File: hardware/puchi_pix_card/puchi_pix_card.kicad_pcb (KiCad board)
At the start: 4 copper layers, 54 x 54 mm, 366 parts, among them J1 USB_C_Receptacle_USB2.0_16P, J2 Conn_01x04, Q101 AO3401A, Q102 AO3401A, Q103 AO3401A, Q104 AO3401A, Q105 AO3401A, Q106 AO3401A, Q107 AO3401A, Q108 AO3401A, Q109 AO3401A, Q110 AO3401A, Q111 AO3401A, Q112 AO3401A, Q113 AO3401A, Q114 AO3401A, Q115 AO3401A, Q116 AO3401A, SW1 VBAT_SW, SW2 SW_Push, SW3 SW_Push, U1 TPS61023DRL, U101 MBI5153GP (R), U102 MBI5153GP (G), U103 MBI5153GP (B), U104 74HCT595, U105 74HCT595, U2 XC6206PxxxMR, U3 STM32G0B1CBTx, U4 XC6206PxxxMR, U5 USBLC6-2SC6, U6 KXTJ3-1057, U7 W25Q64JVSSIQ

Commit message: Swap J2 to JST SH with v1 power pin order (1:GND 2:+3V3S); replace the battery symbol with four pogo-pin contacts (VBAT/GND)
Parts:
- added BT1: POGO BT+, puchi_pix_card:Pogo_YTC1P_D2.0, B.Cu at (151.8, 105.4)
- added BT2: POGO BT+, puchi_pix_card:Pogo_YTC1P_D2.0, B.Cu at (151.8, 108.5)
- added BT3: POGO BT-, puchi_pix_card:Pogo_YTC1P_D2.0, B.Cu at (102.0, 140.5)
- added BT4: POGO BT-, puchi_pix_card:Pogo_YTC1P_D2.0, B.Cu at (102.0, 143.5)
- J2: value Conn_01x04 -> SWD (JST SH 4P); footprint Connector_PinHeader_2.54mm:PinHeader_1x04_P2.54mm_Vertical_SMD_Pin1Left -> JST_SH_SM04B-SRSS-TB_1x04-1MP_P1.00mm_Horizontal
- moved R120 3.83 mm to (143.6, 109.2), turned to 0 degrees
- moved Q102 2.88 mm to (144.6, 105.8)
- moved Q103 2.74 mm to (148.5, 107.2)
- moved R119 2.20 mm to (142.9, 108.1), turned to 0 degrees
- turned J2 to 90 degrees
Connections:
- C14 pad 1: Net-(J2-Pin_1) -> +3V3S
- C5 pad 1: Net-(J2-Pin_1) -> +3V3S
- C6 pad 1: Net-(J2-Pin_1) -> +3V3S
- C7 pad 1: Net-(J2-Pin_1) -> +3V3S
- C8 pad 1: Net-(J2-Pin_1) -> +3V3S
- J2 pad 1: Net-(J2-Pin_1) -> GND
- J2 pad 2: /mcu/SWDIO -> +3V3S
- J2 pad 3: /mcu/BOOT/SWCLK -> /mcu/SWDIO
- J2 pad 4: GND -> /mcu/BOOT/SWCLK
- R13 pad 1: Net-(J2-Pin_1) -> +3V3S
- R14 pad 1: Net-(J2-Pin_1) -> +3V3S
- SW1 pad 2: Net-(BT1-+) -> VBAT
- SW3 pad 2: Net-(J2-Pin_1) -> +3V3S
- U2 pad 2: Net-(J2-Pin_1) -> +3V3S
- U3 pad 4: Net-(J2-Pin_1) -> +3V3S
- U3 pad 5: Net-(J2-Pin_1) -> +3V3S
- U3 pad 6: Net-(J2-Pin_1) -> +3V3S
- U6 pad 10: Net-(J2-Pin_1) -> +3V3S
- U6 pad 11: Net-(J2-Pin_1) -> +3V3S
- U6 pad 3: Net-(J2-Pin_1) -> +3V3S
- U6 pad 7: Net-(J2-Pin_1) -> +3V3S
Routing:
- net +3V3S: track 0.00 -> 107.7 mm, vias 0 -> 5
- net Net-(J2-Pin_1): track 103.2 -> 0.00 mm, vias 5 -> 0
- net VBAT: track 0.00 -> 27.5 mm, vias 0 -> 2
- net GND: track 160.2 -> 166.7 mm, vias 24 -> 25
- net +5V: track 434.1 -> 430.4 mm
- net /mcu/BOOT/SWCLK: track 80.2 -> 83.9 mm
- net /display/COL_R15: track 58.2 -> 61.1 mm
- net /display/ROW2: track 60.2 -> 62.9 mm
- net /mcu/SWDIO: track 45.6 -> 47.5 mm
- net /display/SR_Q1: track 15.3 -> 16.5 mm
- net Net-(U101-OUT14): track 30.5 -> 29.5 mm
- net Net-(U101-OUT15): track 34.0 -> 33.2 mm
- net /display/SR_Q2: track 21.8 -> 21.0 mm

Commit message: Fill LCSC part numbers for JLCPCB assembly; switch the column drivers to MBI5124GP-B (pin 21 GCLK -> /OE, net MBI_OE); R2 133k, in-stock LED/NOR listings
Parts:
- J1: value USB_C_Receptacle_USB2.0_16P -> TYPE-C 16P QTWT
- R2: value 135k -> 133k
- U101: value MBI5153GP (R) -> MBI5124GP-B (R)
- U102: value MBI5153GP (G) -> MBI5124GP-B (G)
- U103: value MBI5153GP (B) -> MBI5124GP-B (B)
- U2, U4: value XC6206PxxxMR -> XC6206P332MR
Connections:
- net GCLK renamed MBI_OE

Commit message: Review fixes: guard the first plane against ISR re-entry, SPI2 8 MHz for the 3.3V chain delay, release the KXTJ3 latched INT, force /OE high on stop; J2 real part name and footprint id; drop MBI5153 leftovers
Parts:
- J2: value SWD (JST SH 4P) -> SWD XDWF-0910-04P (JST SH compatible); footprint JST_SH_SM04B-SRSS-TB_1x04-1MP_P1.00mm_Horizontal -> Connector_JST:JST_SH_SM04B-SRSS-TB_1x04-1MP_P1.00mm_Horizontal
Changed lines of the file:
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@@
 		)
 	)
-	(footprint "JST_SH_SM04B-SRSS-TB_1x04-1MP_P1.00mm_Horizontal"
+	(footprint "Connector_JST:JST_SH_SM04B-SRSS-TB_1x04-1MP_P1.00mm_Horizontal"
 		(layer "B.Cu")
 		(at 103.75 106.61 90)
@@
 			)
 		)
-		(property "Value" "SWD (JST SH 4P)"
+		(property "Value" "SWD XDWF-0910-04P (JST SH compatible)"
 			(at 0 -3.98 270)
 			(layer "B.Fab")

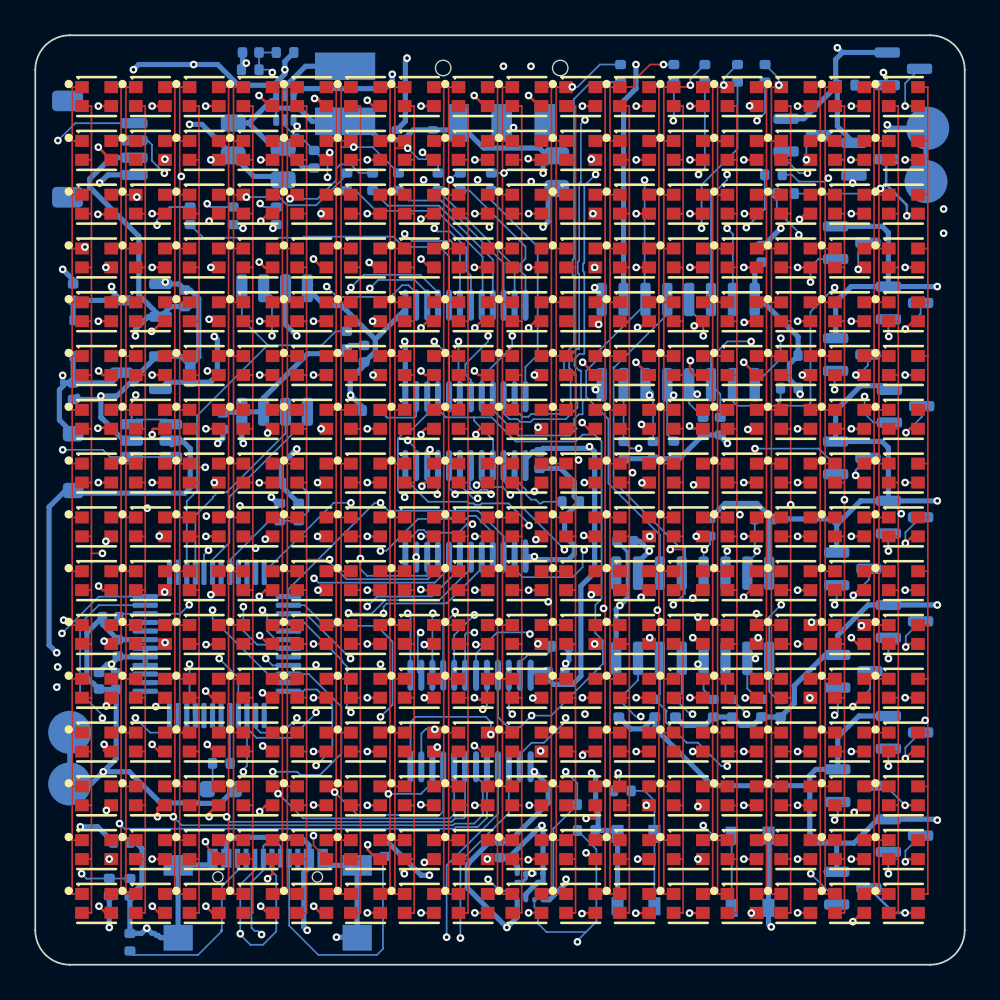
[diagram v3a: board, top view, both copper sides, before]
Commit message: Move SW1 into the +3V3S branch (boost VIN on VBAT) so the 0.1A switch carries only the MCU rail; R101 2.0k / red series 120R for the MBI5124 10mA limit and USB headroom; R9 4.7k; C1 next to U1; In1 GND plane rejoined
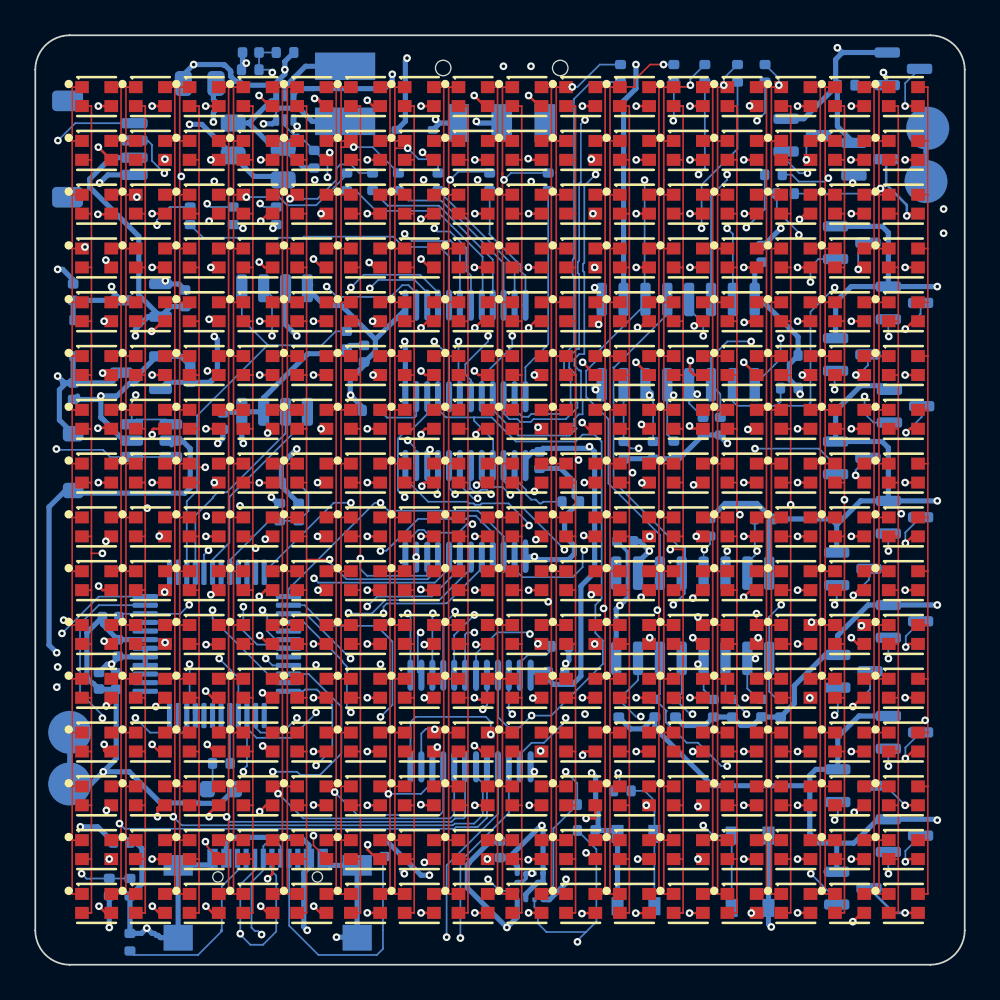
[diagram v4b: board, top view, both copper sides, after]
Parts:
- R101: value 1.8k -> 2.0k
- R105, R106, R107, R108, R109, R110, R111, R112, R113, R114, R115, R116, R117, R118, R119, R120: value 180 -> 120
- R9: value 1k -> 4.7k
- moved C1 21.4 mm to (109.5, 102.8), turned to 180 degrees
- moved R113 3.30 mm to (129.8, 108.5)
- moved R112 1.70 mm to (126.4, 108.5)
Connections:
- C1 pad 1: Net-(D2-A) -> Net-(BT1-Pin_1)
- D2 pad 2: Net-(D2-A) -> /mcu/VBAT_SW
- L1 pad 1: Net-(D2-A) -> Net-(BT1-Pin_1)
- R10 pad 1: Net-(D2-A) -> /mcu/VBAT_SW
- SW1 pad 1: Net-(D2-A) -> /mcu/VBAT_SW
- SW1 pad 2: VBAT -> Net-(BT1-Pin_1)
- U1 pad 3: Net-(D2-A) -> Net-(BT1-Pin_1)
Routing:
- net Net-(D2-A): track 74.0 -> 0.00 mm, vias 3 -> 0
- net /mcu/VBAT_SW: track 0.00 -> 53.9 mm, vias 0 -> 3
- net Net-(BT1-Pin_1): track 0.00 -> 27.9 mm, vias 0 -> 3
- net VBAT: track 27.5 -> 3.14 mm, vias 2 -> 0
- net GND: track 166.7 -> 152.0 mm, vias 25 -> 23
- net SR_SER: track 82.2 -> 68.9 mm, vias 2 -> 3
- net /display/COL_R8: track 56.8 -> 59.2 mm
- net /display/COL_R7: track 56.8 -> 58.5 mm
- net Net-(U101-OUT7): track 9.01 -> 7.69 mm
- net Net-(U101-OUT8): track 13.4 -> 12.5 mm
- net Net-(U101-OUT11): track 36.8 -> 36.1 mm
- net /display/ROW4: track 61.6 -> 60.9 mm
- net /mcu/SWDIO: track 47.5 -> 48.1 mm
